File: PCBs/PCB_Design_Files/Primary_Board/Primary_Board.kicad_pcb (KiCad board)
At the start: 2 copper layers, 0 parts

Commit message: AFE layout, oled+esp libraries
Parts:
- added C1: 1u, Project Footprints:0603_capacitor, B.Cu at (151.5, 86.1)
- added C2: 2.2p, Project Footprints:0603_capacitor, B.Cu at (152.6, 89.2)
- added C3: 1u, Project Footprints:0603_capacitor, B.Cu at (144.8, 92.2)
- added C4: .1u, Project Footprints:0603_capacitor, B.Cu at (140.8, 84.2)
- added C5: 3.9u, Project Footprints:0603_capacitor, B.Cu at (148.0, 93.0)
- added C6: 220n, Project Footprints:0603_capacitor, B.Cu at (134.1, 99.9)
- added C7: 220n, Project Footprints:0603_capacitor, B.Cu at (136.6, 98.4)
- added C8: .1u, Project Footprints:0603_capacitor, B.Cu at (136.1, 90.8)
- added C9: .1u, Project Footprints:0603_capacitor, B.Cu at (151.1, 102.9)
- added LED1: SFH 2704, Project Footprints:SFH2704_LED, B.Cu at (146.2, 81.5)
- added R1: 100k, Project Footprints:0603_resistor, B.Cu at (150.6, 83.6)
- added R10: 35k, Project Footprints:0603_resistor, B.Cu at (145.4, 97.0)
- added R11: 10k, Project Footprints:0603_resistor, B.Cu at (149.0, 97.0)
- added R2: 150k, Project Footprints:0603_resistor, B.Cu at (150.1, 89.2)
- added R3: 100k, Project Footprints:0603_resistor, B.Cu at (139.9, 98.6)
- added R4: 120k, Project Footprints:0603_resistor, B.Cu at (139.9, 102.7)
- added R5: 120k, Project Footprints:0603_resistor, B.Cu at (136.6, 102.7)
- added R6: 1k, Project Footprints:0603_resistor, B.Cu at (142.7, 98.5)
- added R7: 380k, Project Footprints:0603_resistor, B.Cu at (133.8, 93.8)
- added R8: 10k, Project Footprints:0603_resistor, B.Cu at (153.3, 101.4)
- added R9: 10k, Project Footprints:0603_resistor, B.Cu at (152.5, 98.2)
- added U1: OPA381, Project Footprints:OPA381, B.Cu at (146.2, 87.6)
- added U2: TLV9002, Project Footprints:TLV9002, B.Cu at (139.4, 93.0)
- added U3: TLV9002, Project Footprints:TLV9002, B.Cu at (140.4, 87.6)
- added U4: TLV9002, Project Footprints:TLV9002, B.Cu at (147.7, 101.0)
- added U5: MOUDLE-SEEEDUINO-XIAO-ESP32C3, Project Footprints:XIAO_ESP32S3_MODULE, F.Cu at (155.6, 109.0)
- added U6: DM-OLED096-636, Project Footprints:OLED096-636, F.Cu at (146.5, 87.5)
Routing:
- net /AFE/Vref: track 0.00 -> 22.1 mm
- net GND: track 0.00 -> 19.0 mm, vias 0 -> 13
- net Net-(U4-IN1+): track 0.00 -> 19.0 mm
- net /AFE/TIA_Out: track 0.00 -> 17.2 mm
- net Net-(U2-IN2-): track 0.00 -> 17.0 mm, vias 0 -> 2
- net Net-(C5-Pad2): track 0.00 -> 14.6 mm, vias 0 -> 2
- net Net-(U2-IN1+): track 0.00 -> 13.1 mm
- net /AFE/+1.65V: track 0.00 -> 12.0 mm
- net /AFE/PD_Out: track 0.00 -> 11.9 mm
- net Net-(U2-IN1-): track 0.00 -> 11.6 mm
- net Net-(C6-Pad1): track 0.00 -> 7.50 mm
- net Net-(U1-IN+): track 0.00 -> 7.37 mm
- net Net-(U4-IN2+): track 0.00 -> 5.83 mm
- net +3V3: track 0.00 -> 5.56 mm, vias 0 -> 4
- net /AFE/ADC_AC: track 0.00 -> 4.40 mm
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- added copper zone on B.Cu, net +3V3
- added copper zone on In1.Cu, net +3V3
- added copper zone on B.Cu, net /AFE/+1.65V
- added copper zone on In2.Cu, net GND
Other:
- board outline added: 40.3 x 57.1 mm
- copper layers 2 -> 4
- rule pad_to_mask_clearance: 1 -> 0

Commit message: mounting holes
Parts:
- added ?: , , F.Cu at (129.4, 127.0)
- added ? (x3): , , F.Cu at (162.9, 127.0)
- added REF**: MountingHole_2.2mm_M2_DIN965_Pad, MountingHole:MountingHole_2.2mm_M2_DIN965_Pad, F.Cu at (129.4, 127.0)
- added REF**: MountingHole_2.2mm_M2_DIN965_Pad, MountingHole:MountingHole_2.2mm_M2_DIN965_Pad, F.Cu at (162.9, 127.0)
- added REF**: MountingHole_2.2mm_M2_DIN965_Pad, MountingHole:MountingHole_2.2mm_M2_DIN965_Pad, F.Cu at (129.4, 76.8)
- added REF**: MountingHole_2.2mm_M2_DIN965_Pad, MountingHole:MountingHole_2.2mm_M2_DIN965_Pad, F.Cu at (162.9, 76.8)

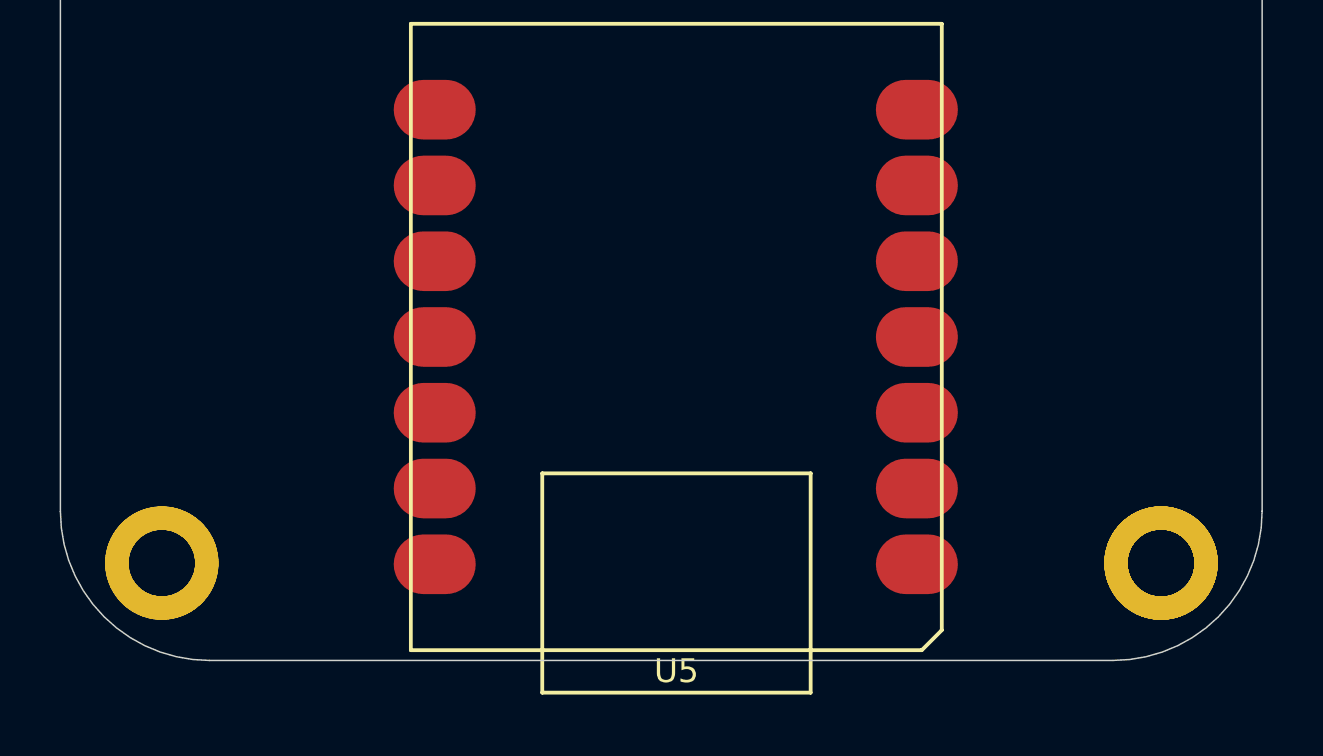
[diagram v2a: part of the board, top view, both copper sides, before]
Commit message: Bandgap/Ptat layout on secondary board. Updated grounded mounting holes on schematic, fix all DRC warnings
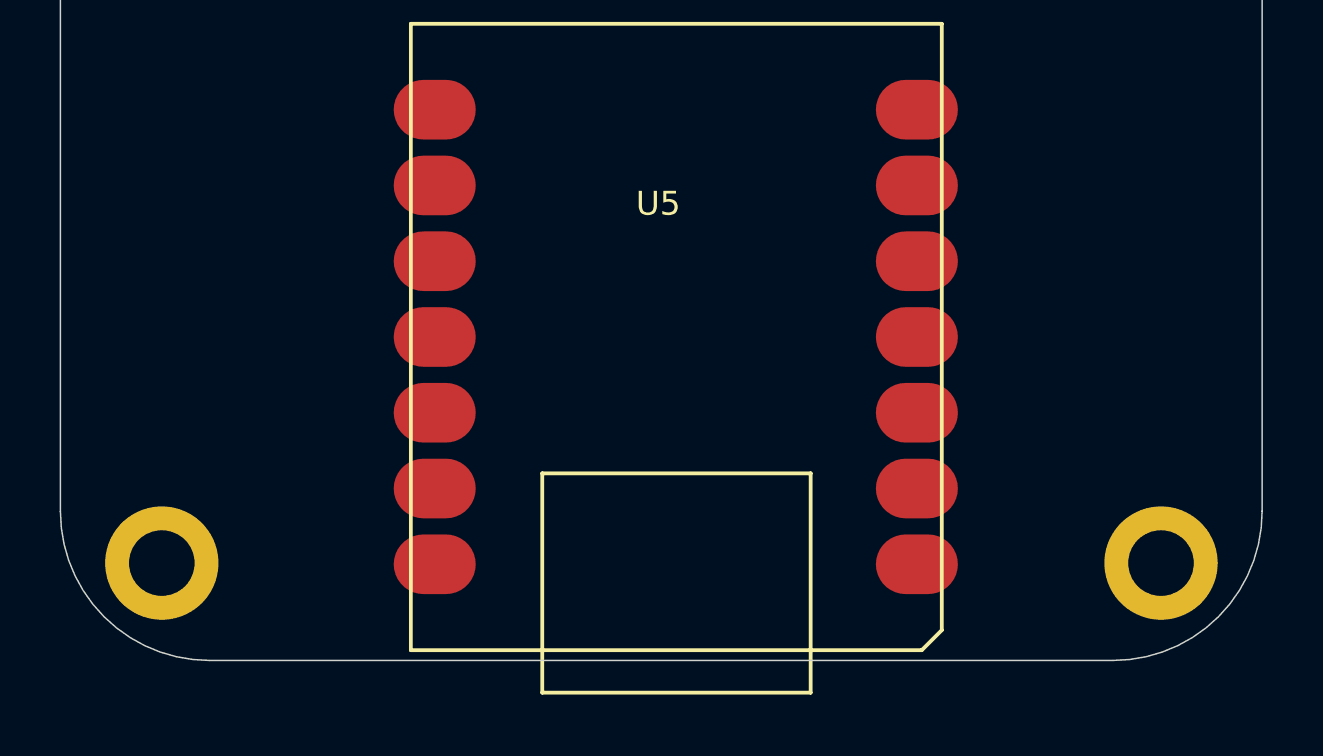
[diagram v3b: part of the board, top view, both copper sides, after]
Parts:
- removed ? (x4): , 
- removed REF** (x4): MountingHole_2.2mm_M2_DIN965_Pad, MountingHole:MountingHole_2.2mm_M2_DIN965_Pad
- added H1: MountingHole_Pad, MountingHole:MountingHole_2.2mm_M2_DIN965_Pad, F.Cu at (129.4, 76.8)
- added H2: MountingHole_Pad, MountingHole:MountingHole_2.2mm_M2_DIN965_Pad, F.Cu at (162.9, 76.8)
- added H3: MountingHole_Pad, MountingHole:MountingHole_2.2mm_M2_DIN965_Pad, F.Cu at (129.4, 127.0)
- added H4: MountingHole_Pad, MountingHole:MountingHole_2.2mm_M2_DIN965_Pad, F.Cu at (162.9, 127.0)

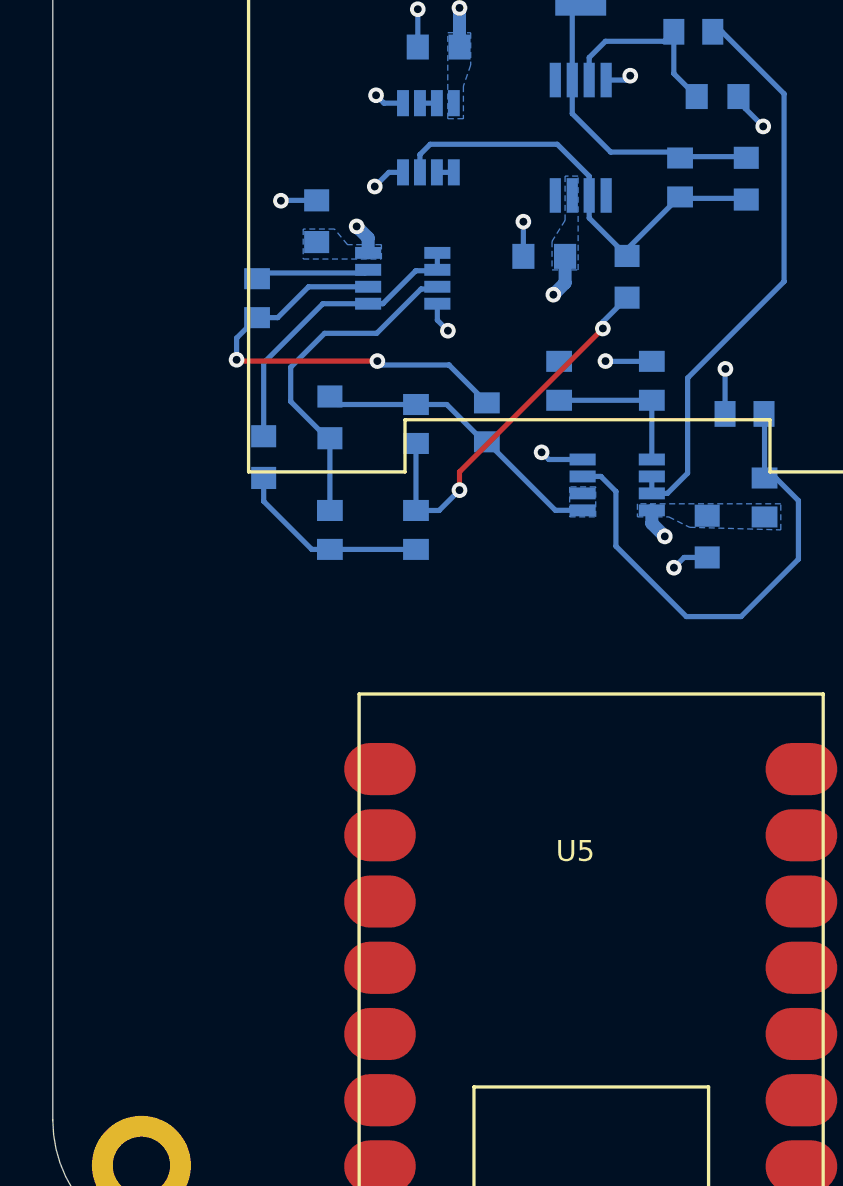
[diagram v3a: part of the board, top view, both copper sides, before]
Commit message: Added header and ffc connector to both boards + update libraries. Updated BOM
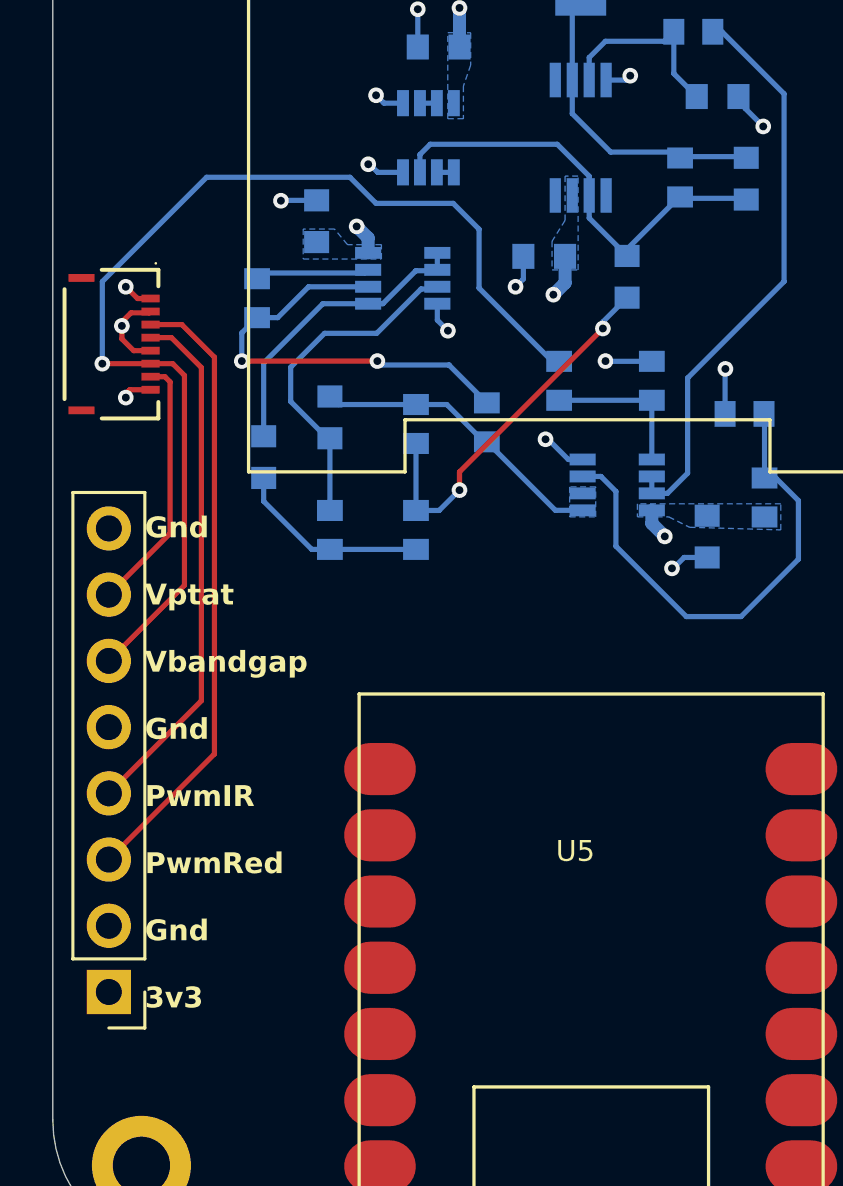
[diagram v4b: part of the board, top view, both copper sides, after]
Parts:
- added J1: Conn_FFC_8pin, Project Footprints:Conn_FFC_8pin, F.Cu at (128.2, 95.5)
- added J2: Conn_01x08_Pin, Connector_PinHeader_2.54mm:PinHeader_1x08_P2.54mm_Vertical, F.Cu at (128.2, 120.4)
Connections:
- R10 pad 1: /AFE/V_bandgap -> /V_bandgap
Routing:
- net /V_bandgap: track 0.00 -> 42.1 mm, vias 0 -> 1
- net /PWM_Red: track 0.00 -> 23.9 mm
- net /PWM_IR: track 0.00 -> 20.2 mm
- net /V_ptat: track 0.00 -> 9.87 mm
- net GND: track 19.0 -> 24.2 mm, vias 13 -> 15
- net +3V3: track 5.56 -> 6.70 mm, vias 4 -> 5
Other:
- board text added: "Gnd Vptat Vbandgap Gnd PwmIR PwmRed Gnd 3v3"

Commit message: Started Layout
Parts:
- added C10: 10nF, Capacitor_SMD:C_0603_1608Metric, F.Cu at (100.3, 118.5)
- added C11: 10nF, Capacitor_SMD:C_0603_1608Metric, F.Cu at (98.7, 122.5)
- added C12: 10nF, Capacitor_SMD:C_0603_1608Metric, F.Cu at (100.3, 121.5)
- added C13: 10nF, Capacitor_SMD:C_0603_1608Metric, F.Cu at (98.7, 125.6)
- added C14: 100nF, Capacitor_SMD:C_0402_1005Metric, F.Cu at (100.5, 124.5)
- added C15: 8pF, Capacitor_SMD:C_0603_1608Metric, F.Cu at (36.7, 64.8)
- added C16: 8pF, Capacitor_SMD:C_0603_1608Metric, F.Cu at (36.7, 67.3)
- added C17: 8pF, Capacitor_SMD:C_0603_1608Metric, F.Cu at (36.7, 69.8)
- added C18: 8pF, Capacitor_SMD:C_0603_1608Metric, F.Cu at (36.7, 72.3)
- added C19: 8pF, Capacitor_SMD:C_0603_1608Metric, F.Cu at (36.7, 74.8)
- added C20: 8pF, Capacitor_SMD:C_0603_1608Metric, F.Cu at (40.7, 54.7)
- added C21: 8pF, Capacitor_SMD:C_0603_1608Metric, F.Cu at (40.7, 57.2)
- added C22: 8pF, Capacitor_SMD:C_0603_1608Metric, F.Cu at (40.7, 59.8)
- added C23: 8pF, Capacitor_SMD:C_0603_1608Metric, F.Cu at (40.7, 62.3)
- added C24: 8pF, Capacitor_SMD:C_0603_1608Metric, F.Cu at (40.7, 64.8)
- added C25: 8pF, Capacitor_SMD:C_0603_1608Metric, F.Cu at (40.7, 67.3)
- added C26: 8pF, Capacitor_SMD:C_0603_1608Metric, F.Cu at (40.7, 69.8)
- added C27: 8pF, Capacitor_SMD:C_0603_1608Metric, F.Cu at (40.7, 72.3)
- added C28: 8pF, Capacitor_SMD:C_0603_1608Metric, F.Cu at (40.7, 74.8)
- added C29: 8pF, Capacitor_SMD:C_0603_1608Metric, F.Cu at (44.7, 54.7)
- added C30: 4pF, Capacitor_SMD:C_0603_1608Metric, F.Cu at (44.7, 57.2)
- added C31: 2pF, Capacitor_SMD:C_0603_1608Metric, F.Cu at (44.7, 59.8)
- added C32: 1pF, Capacitor_SMD:C_0603_1608Metric, F.Cu at (44.7, 62.3)
- added C33: 8pF, Capacitor_SMD:C_0603_1608Metric, F.Cu at (44.7, 64.8)
- added C34: 8pF, Capacitor_SMD:C_0603_1608Metric, F.Cu at (44.7, 67.3)
- added C35: 8pF, Capacitor_SMD:C_0603_1608Metric, F.Cu at (44.7, 69.8)
- added C36: 8pF, Capacitor_SMD:C_0603_1608Metric, F.Cu at (44.7, 72.3)
- added C37: 8pF, Capacitor_SMD:C_0603_1608Metric, F.Cu at (44.7, 74.8)
- added C38: 8pF, Capacitor_SMD:C_0603_1608Metric, F.Cu at (48.7, 54.7)
- added C39: 8pF, Capacitor_SMD:C_0603_1608Metric, F.Cu at (48.7, 57.2)
- added C40: 8pF, Capacitor_SMD:C_0603_1608Metric, F.Cu at (48.7, 59.8)
- added C41: 8pF, Capacitor_SMD:C_0603_1608Metric, F.Cu at (48.7, 62.3)
- added C42: 8pF, Capacitor_SMD:C_0603_1608Metric, F.Cu at (48.7, 64.8)
- added C43: 8pF, Capacitor_SMD:C_0603_1608Metric, F.Cu at (48.7, 67.3)
- added C44: 8pF, Capacitor_SMD:C_0603_1608Metric, F.Cu at (48.7, 69.8)
- added C45: 8pF, Capacitor_SMD:C_0603_1608Metric, F.Cu at (48.7, 72.3)
- added C46: 8pF, Capacitor_SMD:C_0603_1608Metric, F.Cu at (48.7, 74.8)
- added C47: 8pF, Capacitor_SMD:C_0603_1608Metric, F.Cu at (52.7, 54.7)
- added C48: 4pF, Capacitor_SMD:C_0603_1608Metric, F.Cu at (52.7, 57.2)
- added C49: 2pF, Capacitor_SMD:C_0603_1608Metric, F.Cu at (52.7, 59.8)
- added C50: 1pF, Capacitor_SMD:C_0603_1608Metric, F.Cu at (52.7, 62.3)
- added C51: 1pF, Capacitor_SMD:C_0603_1608Metric, F.Cu at (52.7, 64.8)
- added C52: 1pF, Capacitor_SMD:C_0603_1608Metric, F.Cu at (52.7, 67.3)
- added C53: 100nF, Capacitor_SMD:C_0402_1005Metric, F.Cu at (101.7, 98.7)
- added C54: 100nF, Capacitor_SMD:C_0402_1005Metric, F.Cu at (101.7, 100.7)
- added C55: 100nF, Capacitor_SMD:C_0402_1005Metric, F.Cu at (101.7, 102.6)
- added C56: 100nF, Capacitor_SMD:C_0402_1005Metric, F.Cu at (104.5, 96.7)
- added C57: 100nF, Capacitor_SMD:C_0402_1005Metric, F.Cu at (104.5, 98.7)
- added C58: 100nF, Capacitor_SMD:C_0402_1005Metric, F.Cu at (104.5, 100.7)
- added C59: 100nF, Capacitor_SMD:C_0402_1005Metric, F.Cu at (104.5, 102.6)
- added C60: 100nF, Capacitor_SMD:C_0402_1005Metric, F.Cu at (107.4, 96.7)
- added C61: 100nF, Capacitor_SMD:C_0402_1005Metric, F.Cu at (107.4, 98.7)
- added C62: 100nF, Capacitor_SMD:C_0402_1005Metric, F.Cu at (107.4, 100.7)
- added C63: 100nF, Capacitor_SMD:C_0402_1005Metric, F.Cu at (107.4, 102.6)
- added C64: 100nF, Capacitor_SMD:C_0402_1005Metric, F.Cu at (110.3, 96.7)
- added C65: 100nF, Capacitor_SMD:C_0402_1005Metric, F.Cu at (110.3, 98.7)
- added C66: 1uF, Capacitor_SMD:C_0402_1005Metric, F.Cu at (95.1, 128.8)
- added C67: 1uF, Capacitor_SMD:C_0402_1005Metric, F.Cu at (97.3, 126.1)
- added R12: 100, Resistor_SMD:R_0402_1005Metric, F.Cu at (98.5, 120.5)
- added R13: 100, Resistor_SMD:R_0402_1005Metric, F.Cu at (97.0, 123.6)
- added R14: 100, Resistor_SMD:R_0402_1005Metric, F.Cu at (98.5, 119.5)
- added R15: 100, Resistor_SMD:R_0402_1005Metric, F.Cu at (97.0, 124.6)
- added R16: 10k, Resistor_SMD:R_0402_1005Metric, F.Cu at (101.6, 117.6)
- added SR1: 74HC595D, Package_SO:SOIC-16_3.9x9.9mm_P1.27mm, F.Cu at (87.5, 101.6)
- added SR2: 74HC595D, Package_SO:SOIC-16_3.9x9.9mm_P1.27mm, F.Cu at (96.0, 101.6)
- added U11: TMUX1104DGSR, Package_SO:VSSOP-10_3x3mm_P0.5mm, F.Cu at (103.0, 121.8)
- added U12: TMUX1133PWR, Package_SO:TSSOP-16_4.4x5mm_P0.65mm, F.Cu at (78.9, 83.0)
- added U13: TMUX1133PWR, Package_SO:TSSOP-16_4.4x5mm_P0.65mm, F.Cu at (78.9, 89.6)
- added U14: TMUX1133PWR, Package_SO:TSSOP-16_4.4x5mm_P0.65mm, F.Cu at (78.9, 96.2)
- added U15: TMUX1133PWR, Package_SO:TSSOP-16_4.4x5mm_P0.65mm, F.Cu at (78.9, 102.8)
- added U7: REF3333AIDBZR, Package_TO_SOT_SMD:SOT-23-3, F.Cu at (95.1, 126.2)
- added U8: TMUX1133PWR, Package_SO:TSSOP-16_4.4x5mm_P0.65mm, F.Cu at (78.9, 76.4)
- added U9: MCP6561T-E/OT, Package_TO_SOT_SMD:SOT-23-5_HandSoldering, F.Cu at (106.3, 90.1)
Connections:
- net /AFE/ADC_AC renamed /ADC/ADC_Input1
- net /AFE/ADC_DC renamed /ADC/ADC_Input2
- J1 pad 2: GND -> +5V
- J2 pad 2: GND -> +5V

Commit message: .
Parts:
- moved U8 24.0 mm to (63.5, 94.8)
- moved U12 24.0 mm to (63.6, 101.4)
- moved U13 24.0 mm to (63.6, 108.0)
- moved U14 24.0 mm to (63.6, 114.6)
- moved U15 24.0 mm to (63.6, 121.2)
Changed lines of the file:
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@@
 	(footprint "Package_SO:TSSOP-16_4.4x5mm_P0.65mm"
 		(layer "F.Cu")
-		(at 78.949 83.02)
+		(at 63.5685 101.417)
 		(descr "TSSOP, 16 Pin (https://www.jedec.org/document_search?search_api_views_fulltext=MO-153), generated with kicad-footprint-generator ipc_gullwing_generator.py")
 		(tags "TSSOP SO JEDEC-MO-153-AB Texas_PW0016A Microchip-ST Toshiba-TSSOP16-P-0044-0.65A NXP-SOT403-1 Infineon-P-TSSOP-16-800")
@@
 	(footprint "Package_SO:TSSOP-16_4.4x5mm_P0.65mm"
 		(layer "F.Cu")
-		(at 78.949 89.61)
+		(at 63.5685 108.007)
 		(descr "TSSOP, 16 Pin (https://www.jedec.org/document_search?search_api_views_fulltext=MO-153), generated with kicad-footprint-generator ipc_gullwing_generator.py")
 		(tags "TSSOP SO JEDEC-MO-153-AB Texas_PW0016A Microchip-ST Toshiba-TSSOP16-P-0044-0.65A NXP-SOT403-1 Infineon-P-TSSOP-16-800")
@@
 	(footprint "Package_SO:TSSOP-16_4.4x5mm_P0.65mm"
 		(layer "F.Cu")
-		(at 78.949 102.79)
+		(at 63.5685 121.187)
 		(descr "TSSOP, 16 Pin (https://www.jedec.org/document_search?search_api_views_fulltext=MO-153), generated with kicad-footprint-generator ipc_gullwing_generator.py")
 		(tags "TSSOP SO JEDEC-MO-153-AB Texas_PW0016A Microchip-ST Toshiba-TSSOP16-P-0044-0.65A NXP-SOT403-1 Infineon-P-TSSOP-16-800")
@@
 	(footprint "Package_SO:TSSOP-16_4.4x5mm_P0.65mm"
 		(layer "F.Cu")
-		(at 78.949 96.2)
+		(at 63.5685 114.597)
 		(descr "TSSOP, 16 Pin (https://www.jedec.org/document_search?search_api_views_fulltext=MO-153), generated with kicad-footprint-generator ipc_gullwing_generator.py")
 		(tags "TSSOP SO JEDEC-MO-153-AB Texas_PW0016A Microchip-ST Toshiba-TSSOP16-P-0044-0.65A NXP-SOT403-1 Infineon-P-TSSOP-16-800")
@@
 	(footprint "Package_SO:TSSOP-16_4.4x5mm_P0.65mm"
 		(layer "F.Cu")
-		(at 78.949 76.43)
+		(at 63.463 94.827)
 		(descr "TSSOP, 16 Pin (https://www.jedec.org/document_search?search_api_views_fulltext=MO-153), generated with kicad-footprint-generator ipc_gullwing_generator.py")
 		(tags "TSSOP SO JEDEC-MO-153-AB Texas_PW0016A Microchip-ST Toshiba-TSSOP16-P-0044-0.65A NXP-SOT403-1 Infineon-P-TSSOP-16-800")
